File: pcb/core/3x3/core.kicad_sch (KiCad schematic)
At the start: 29 parts, among them J1 Conn_01x11, J2 Conn_01x11, J3 Conn_01x04, SW1 SW_Push_45deg, SW10 RotaryEncoder_Switch, SW11 RotaryEncoder_Switch, SW2 SW_Push_45deg, SW3 SW_Push_45deg, SW4 SW_Push_45deg, SW5 SW_Push_45deg, SW6 SW_Push_45deg, SW7 SW_Push_45deg, SW8 SW_Push_45deg, SW9 SW_Push_45deg, U1 Helios

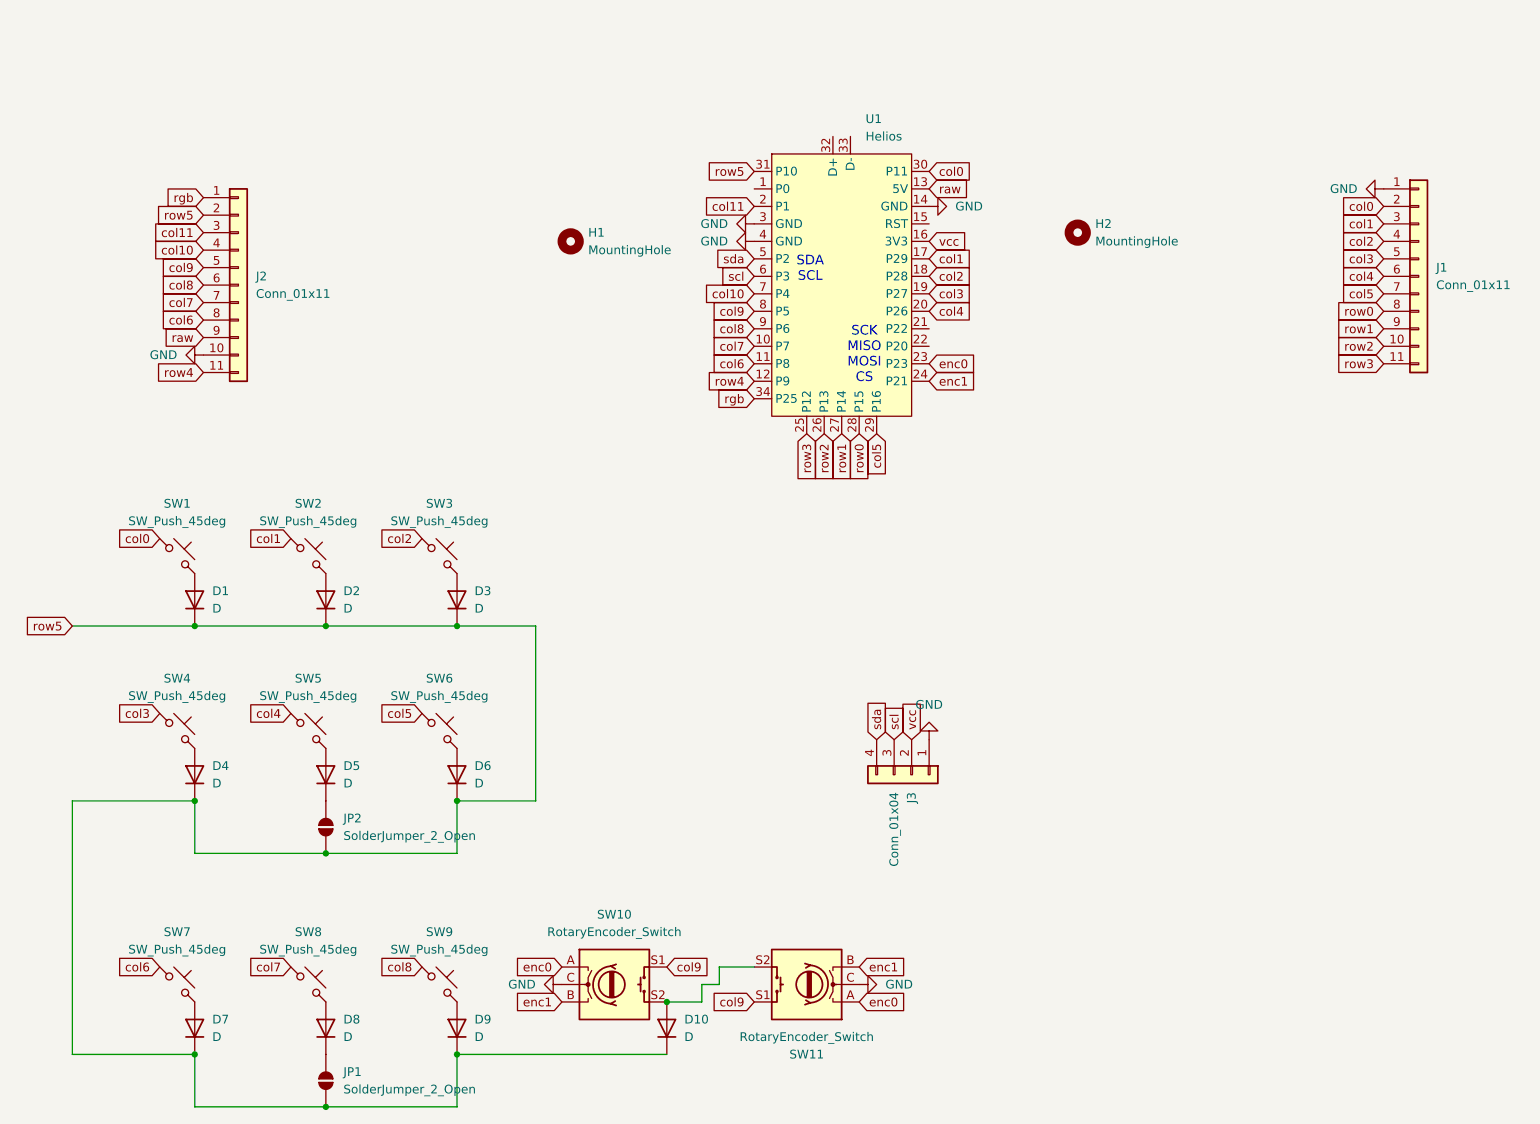
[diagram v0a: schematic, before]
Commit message: added two additional encoders
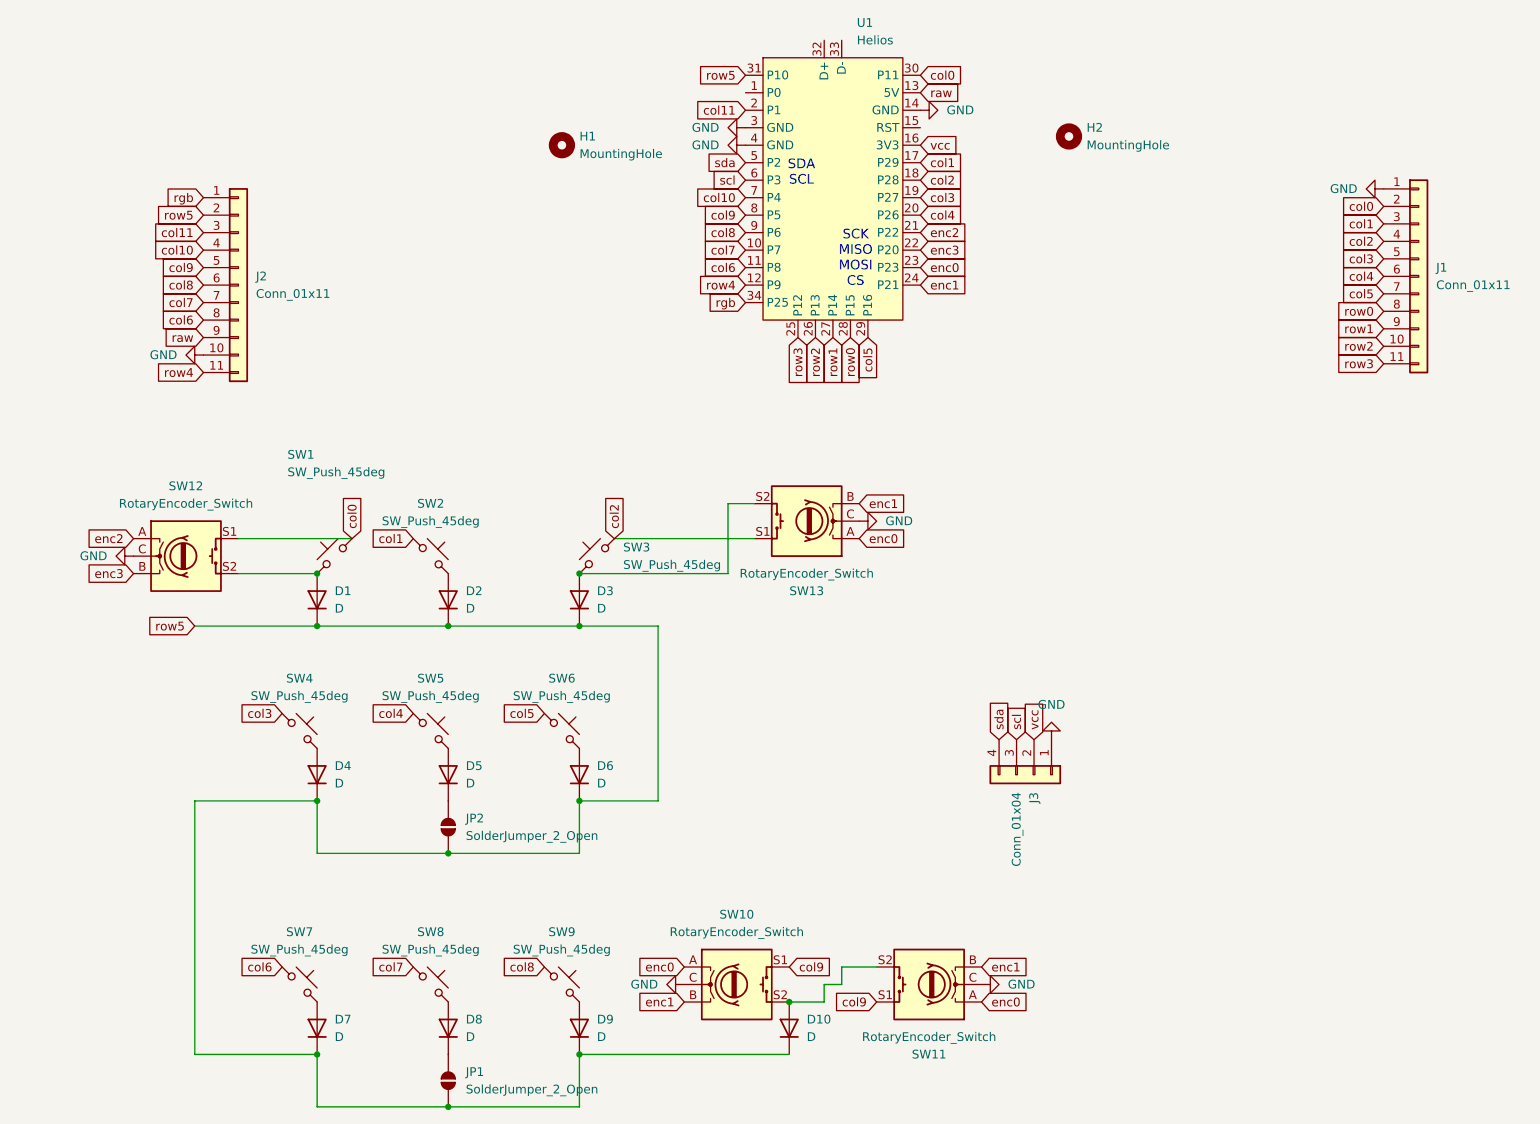
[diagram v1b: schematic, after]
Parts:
- added SW12, SW13: RotaryEncoder_Switch, PCM_marbastlib-various:ROT_Alps_EC11E-Switch, symbol Device:RotaryEncoder_Switch
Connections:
- net GND: now also SW12.C, SW13.C
- net col0: now also SW1.2, SW12.S1; no longer SW1.1
- net col2: now also SW3.2, SW13.S1; no longer SW3.1
- net enc0: now also SW13.A
- net enc1: now also SW13.B
- net at D3.2 (A): now also SW3.1, SW13.S2; no longer SW3.2
- net enc2: now reaches U1.21 (P22)
- net enc2: now also SW12.A
- net enc3: now reaches U1.22 (P20)
- net enc3: now also SW12.B
- net at D1.2 (A): now also SW1.1, SW12.S2; no longer SW1.2
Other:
- moved on the sheet: D1, D10, D2, D3, D4, D5, D6, D7, D8, D9, H1, H2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
